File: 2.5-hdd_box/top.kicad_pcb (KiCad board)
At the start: 2 copper layers, 120 x 105.4 mm, 10 parts

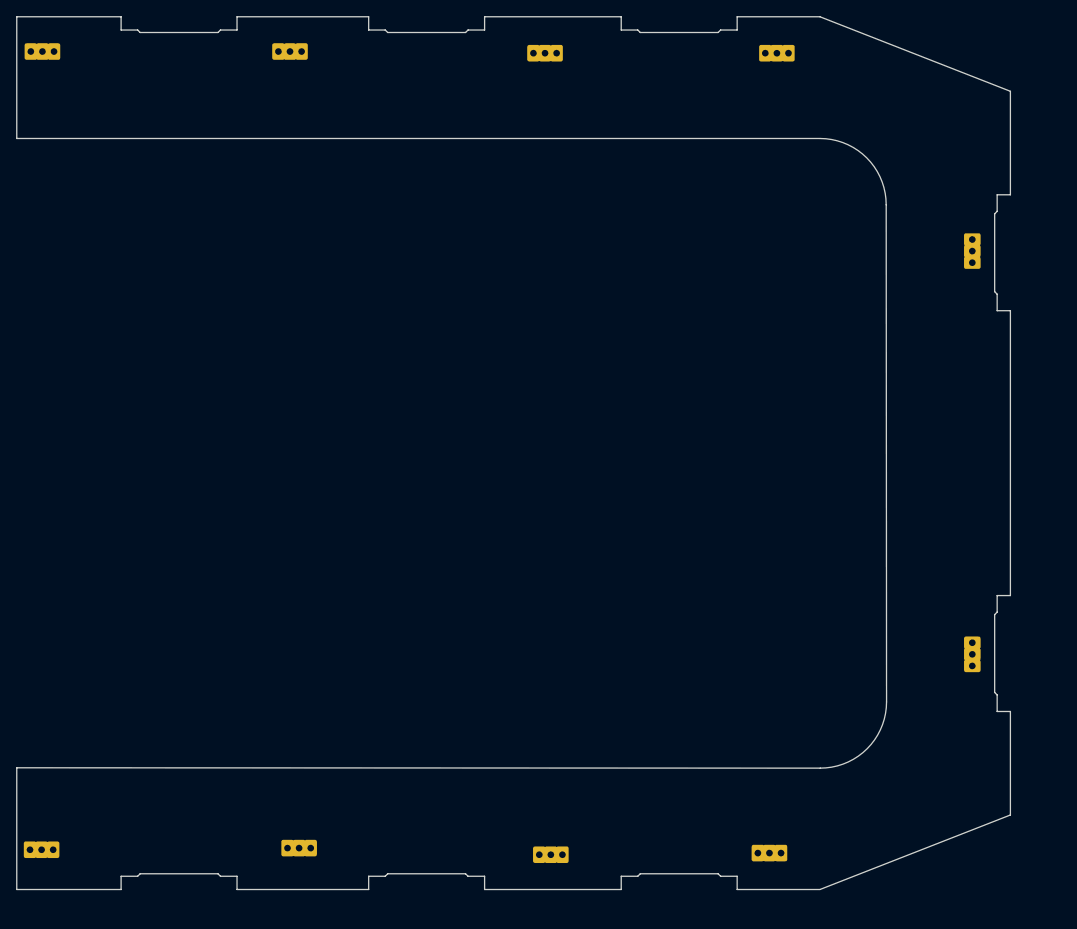
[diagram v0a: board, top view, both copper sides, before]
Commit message: 2.5-hdd_box: cut on bottom for usb-sata board, better placement of soldier pads
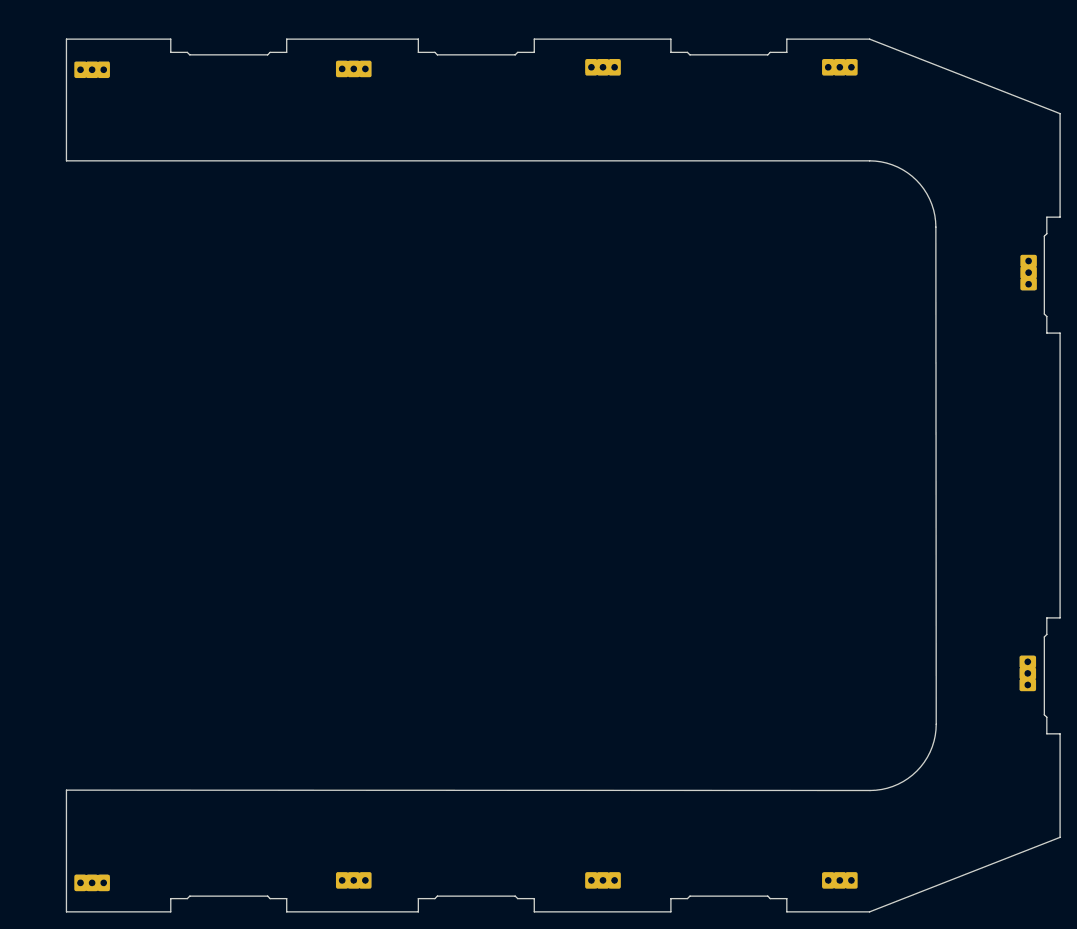
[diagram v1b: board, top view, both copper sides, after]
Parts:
- removed the REF** at (107.9, 132.6)
- removed the REF** at (77.5, 131.8)
- removed the REF** at (135.2, 35.8)
- removed the REF** at (46.5, 35.6)
- removed the REF** at (76.4, 35.6)
- removed the REF** at (107.2, 35.8)
- removed the REF** at (158.7, 108.3)
- removed the REF** at (158.7, 59.6)
- removed the REF** at (46.4, 132.0)
- removed the REF** at (134.3, 132.4)
- added REF**: soldpad, Local:soldpad, F.Cu at (165.4, 110.6)
- added REF**: soldpad, Local:soldpad, F.Cu at (142.8, 135.7)
- added REF**: soldpad, Local:soldpad, F.Cu at (114.2, 37.5)
- added REF**: soldpad, Local:soldpad, F.Cu at (84.1, 37.7)
- added REF**: soldpad, Local:soldpad, F.Cu at (165.5, 62.2)
- added REF**: soldpad, Local:soldpad, F.Cu at (52.5, 136.0)
- added REF**: soldpad, Local:soldpad, F.Cu at (84.1, 135.7)
- added REF**: soldpad, Local:soldpad, F.Cu at (142.8, 37.5)
- added REF**: soldpad, Local:soldpad, F.Cu at (52.5, 37.8)
- added REF**: soldpad, Local:soldpad, F.Cu at (114.2, 135.7)
